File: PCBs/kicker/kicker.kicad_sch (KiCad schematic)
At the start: 1 part, among them Q1 CSD19534Q5A

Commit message: kicker actual start
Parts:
- added C1: 100n, Capacitor_SMD:C_1206_3216Metric, symbol Device:C
- added C2: 4.7u, Capacitor_SMD:C_1206_3216Metric, symbol Device:C
- added C3, C4, C5, C6: 3300u, Capacitor_THT:CP_Radial_D18.0mm_P7.50mm, symbol Device:C_Polarized
- added R1: 2, Resistor_SMD:R_0805_2012Metric, symbol Device:R
- added R2, R3: 10k, Resistor_SMD:R_0603_1608Metric, symbol Device:R
- added R4: 100, Resistor_SMD:R_0603_1608Metric, symbol Device:R
- added U1: UCC27624DR, UCC27624DR:SOIC127P599X175-8N, symbol UCC27624DR:UCC27624DR
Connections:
- net GND: now reaches Q1.1 (S), Q1.2 (S), Q1.3 (S)
- net GND: now also C1.2, C2.2, R2.2, R3.2, U1.3 (GND), U1.4 (INB), U1.8 (ENB)
- net outFET: now reaches Q1.4 (G)
- net outFET: now also R1.2, R3.1
- net SOLout: now reaches Q1.5 (D)
- new net: R2.1, R4.1, U1.2 (INA)
- new net: R1.1, U1.7 (OUTA)
- new net VCC: C1.1, C2.1, U1.1 (ENA), U1.6 (VDD)
- new net mcuDrive: R4.2
- no-connect marks 0 -> 1
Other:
- moved on the sheet: Q1

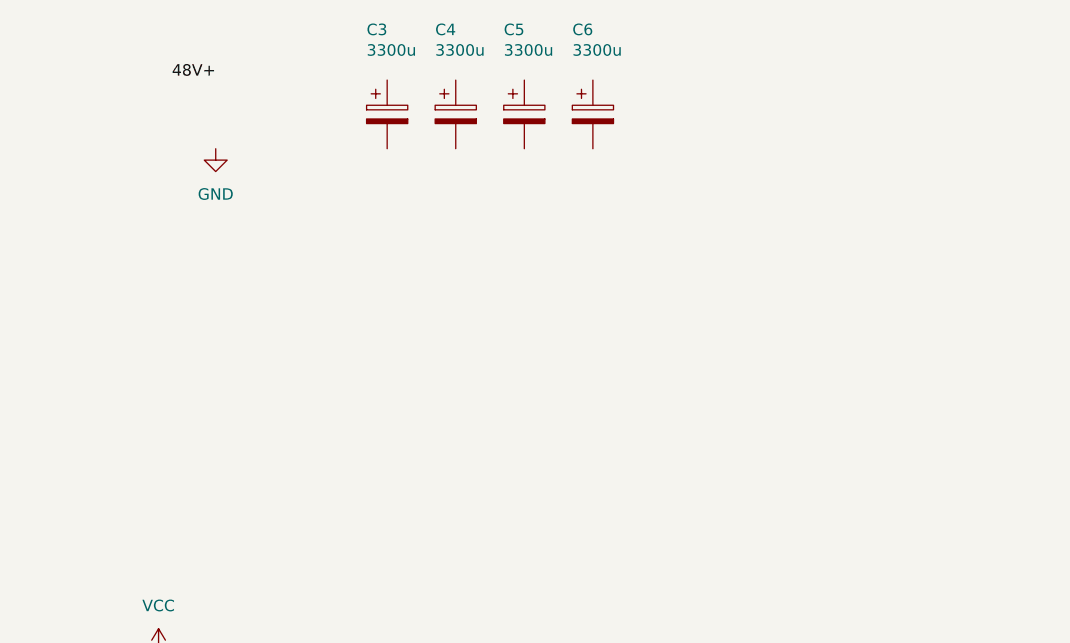
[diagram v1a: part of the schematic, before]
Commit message: fix driver footprint
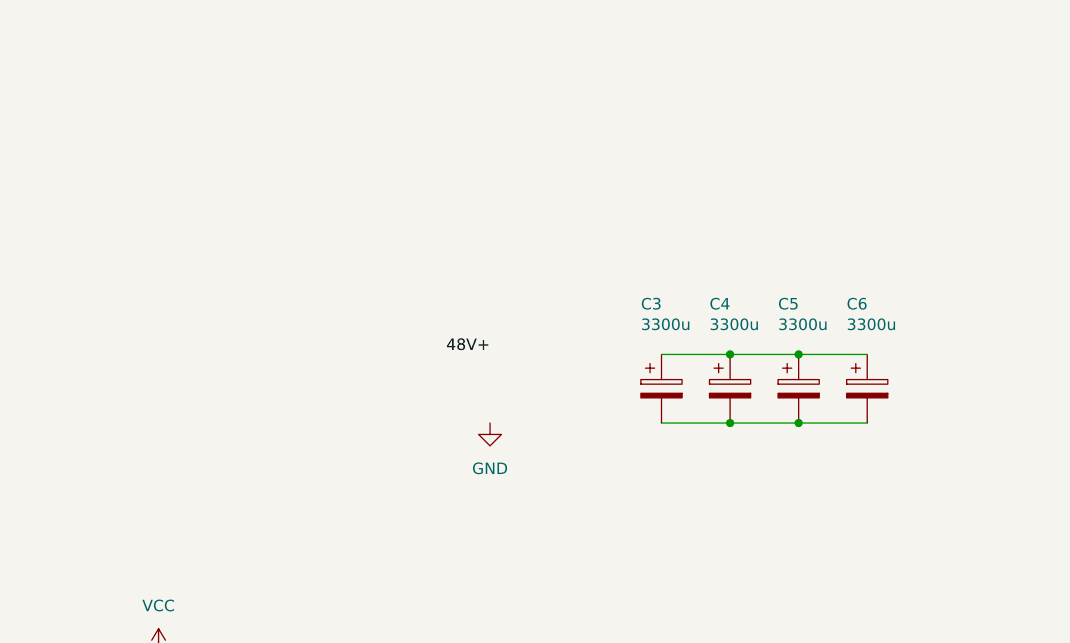
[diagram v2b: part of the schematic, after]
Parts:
- U1: footprint UCC27624DR:SOIC127P599X175-8N -> SOIC127P599X175-8N
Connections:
- net at C6.1: now also C3.1, C4.1, C5.1
- net at C6.2: now also C3.2, C4.2, C5.2
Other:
- moved on the sheet: C3, C4, C5, C6
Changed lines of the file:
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@@
+	)
+	(junction
+		(at 176.53 74.93)
+		(diameter 0)
+		(color 0 0 0 0)
+	)
+	(junction
+		(at 168.91 67.31)
+		(diameter 0)
+		(color 0 0 0 0)
 	)
 	(junction
@@
 	)
 	(junction
+		(at 168.91 74.93)
+		(diameter 0)
+		(color 0 0 0 0)
+	)
+	(junction
 		(at 88.9 156.21)
 		(diameter 0)
@@
 		(color 0 0 0 0)
 	)
+	(junction
+		(at 176.53 67.31)
+		(diameter 0)
+		(color 0 0 0 0)
+	)
 	(no_connect
 		(at 120.65 120.65)
@@
 	(wire
 		(pts
+			(xy 176.53 74.93) (xy 184.15 74.93)
+		)
+		(stroke
+			(width 0)
+			(type default)
+		)
+	)
+	(wire
+		(pts
 			(xy 109.22 156.21) (xy 123.19 156.21)
 		)
@@
 	(wire
 		(pts
+			(xy 161.29 74.93) (xy 168.91 74.93)
+		)
+		(stroke
+			(width 0)
+			(type default)
+		)
+	)
+	(wire
+		(pts
+			(xy 168.91 67.31) (xy 176.53 67.31)
+		)
+		(stroke
+			(width 0)
+			(type default)
+		)
+	)
+	(wire
+		(pts
 			(xy 105.41 146.05) (xy 105.41 144.78)
 		)
@@
 	(wire
 		(pts
+			(xy 168.91 74.93) (xy 176.53 74.93)
+		)
+		(stroke
+			(width 0)
+			(type default)
+		)
+	)
+	(wire
+		(pts
 			(xy 87.63 101.6) (xy 87.63 118.11)
 		)
@@
 	(wire
 		(pts
+			(xy 176.53 67.31) (xy 184.15 67.31)
+		)
+		(stroke
+			(width 0)
+			(type default)
+		)
+	)
+	(wire
+		(pts
+			(xy 161.29 67.31) (xy 168.91 67.31)
+		)
+		(stroke
+			(width 0)
+			(type default)
+		)
+	)
+	(wire
+		(pts
 			(xy 101.6 156.21) (xy 105.41 156.21)
 		)
@@
 	)
 	(label "48V+"
-		(at 111.76 36.83 180)
+		(at 142.24 67.31 180)
 		(effects
 			(font
@@
 	(symbol
 		(lib_id "Device:C_Polarized")
-		(at 153.67 40.64 0)
+		(at 184.15 71.12 0)
 		(unit 1)
 		(exclude_from_sim no)
@@
 		(dnp no)
 		(property "Reference" "C6"
-			(at 151.384 31.242 0)
+			(at 181.864 61.722 0)
 			(effects
 				(font
@@
 		)
 		(property "Value" "3300u"
-			(at 151.384 33.528 0)
+			(at 181.864 64.008 0)
 			(effects
 				(font
@@
 		)
 		(property "Footprint" "Capacitor_THT:CP_Radial_D18.0mm_P7.50mm"
-			(at 154.6352 44.45 0)
+			(at 185.1152 74.93 0)
 			(effects
 				(font
@@
 		)
 		(property "Datasheet" "~"
-			(at 153.67 40.64 0)
+			(at 184.15 71.12 0)
 			(effects
 				(font
@@
 		)
 		(property "Description" "Polarized capacitor"
-			(at 153.67 40.64 0)
+			(at 184.15 71.12 0)
 			(effects
 				(font
@@
 	(symbol
 		(lib_id "Device:C_Polarized")
-		(at 130.81 40.64 0)
+		(at 161.29 71.12 0)
 		(unit 1)
 		(exclude_from_sim no)
@@
 		(dnp no)
 		(property "Reference" "C3"
-			(at 128.524 31.242 0)
+			(at 159.004 61.722 0)
 			(effects
 				(font
@@
 		)
 		(property "Value" "3300u"
-			(at 128.524 33.528 0)
+			(at 159.004 64.008 0)
 			(effects
 				(font
@@
 		)
 		(property "Footprint" "Capacitor_THT:CP_Radial_D18.0mm_P7.50mm"
-			(at 131.7752 44.45 0)
+			(at 162.2552 74.93 0)
 			(effects
 				(font
@@
 		)
 		(property "Datasheet" "~"
-			(at 130.81 40.64 0)
+			(at 161.29 71.12 0)
 			(effects
 				(font
@@
 		)
 		(property "Description" "Polarized capacitor"
-			(at 130.81 40.64 0)
+			(at 161.29 71.12 0)
 			(effects
 				(font
@@
 			)
 		)
-		(property "Footprint" "UCC27624DR:SOIC127P599X175-8N"
+		(property "Footprint" "SOIC127P599X175-8N"
 			(at 105.41 123.19 0)
 			(effects
@@
 	(symbol
 		(lib_id "Device:C_Polarized")
-		(at 146.05 40.64 0)
+		(at 176.53 71.12 0)
 		(unit 1)
 		(exclude_from_sim no)
@@
 		(dnp no)
 		(property "Reference" "C5"
-			(at 143.764 31.242 0)
+			(at 174.244 61.722 0)
 			(effects
 				(font
@@
 		)
 		(property "Value" "3300u"
-			(at 143.764 33.528 0)
+			(at 174.244 64.008 0)
 			(effects
 				(font
@@
 		)
 		(property "Footprint" "Capacitor_THT:CP_Radial_D18.0mm_P7.50mm"
-			(at 147.0152 44.45 0)
+			(at 177.4952 74.93 0)
 			(effects
 				(font
@@
 		)
 		(property "Datasheet" "~"
-			(at 146.05 40.64 0)
+			(at 176.53 71.12 0)
 			(effects
 				(font
@@
 		)
 		(property "Description" "Polarized capacitor"
-			(at 146.05 40.64 0)
+			(at 176.53 71.12 0)
 			(effects
 				(font
@@
 	(symbol
 		(lib_id "power:GND")
-		(at 111.76 44.45 0)
+		(at 142.24 74.93 0)
 		(unit 1)
 		(exclude_from_sim no)
@@
 		(fields_autoplaced yes)
 		(property "Reference" "#PWR05"
-			(at 111.76 50.8 0)
+			(at 142.24 81.28 0)
 			(effects
 				(font
@@
 		)
 		(property "Value" "GND"
-			(at 111.76 49.53 0)
+			(at 142.24 80.01 0)
 			(effects
 				(font
@@
 		)
 		(property "Footprint" ""
-			(at 111.76 44.45 0)
+			(at 142.24 74.93 0)
 			(effects
 				(font
@@
 		)
 		(property "Datasheet" ""
-			(at 111.76 44.45 0)
+			(at 142.24 74.93 0)
 			(effects
 				(font
@@
 		)
 		(property "Description" "Power symbol creates a global label with name \"GND\" , ground"
-			(at 111.76 44.45 0)
+			(at 142.24 74.93 0)
 			(effects
 				(font
@@
 	(symbol
 		(lib_id "Device:C_Polarized")
-		(at 138.43 40.64 0)
+		(at 168.91 71.12 0)
 		(unit 1)
 		(exclude_from_sim no)
@@
 		(dnp no)
 		(property "Reference" "C4"
-			(at 136.144 31.242 0)
+			(at 166.624 61.722 0)
 			(effects
 				(font
@@
 		)
 		(property "Value" "3300u"
-			(at 136.144 33.528 0)
+			(at 166.624 64.008 0)
 			(effects
 				(font
@@
 		)
 		(property "Footprint" "Capacitor_THT:CP_Radial_D18.0mm_P7.50mm"
-			(at 139.3952 44.45 0)
+			(at 169.8752 74.93 0)
 			(effects
 				(font
@@
 		)
 		(property "Datasheet" "~"
-			(at 138.43 40.64 0)
+			(at 168.91 71.12 0)
 			(effects
 				(font
@@
 		)
 		(property "Description" "Polarized capacitor"
-			(at 138.43 40.64 0)
-			(effects
-				(font
+			(at 168.91 71.12 0)
+			(effects
+				(font

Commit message: kicker v0.1
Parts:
- added J1: Conn_01x02_Socket, Connector_JST:JST_XH_S2B-XH-A-1_1x02_P2.50mm_Horizontal, symbol Connector:Conn_01x02_Socket
- added J2: Conn_01x04_Socket, Connector_JST:JST_XH_S4B-XH-A-1_1x04_P2.50mm_Horizontal, symbol Connector:Conn_01x04_Socket
- added J3, J4: Conn_01x01_Socket, Connector_Wire:SolderWirePad_1x01_SMD_5x10mm, symbol Connector:Conn_01x01_Socket
- added Q2: IRF540N, Package_TO_SOT_THT:TO-220-3_Horizontal_TabDown, symbol Transistor_FET:IRF540N
- added R5: 100, Package_TO_SOT_SMD:TO-263-2, symbol Device:R
- added R6, R9: 10k, Resistor_SMD:R_0603_1608Metric, symbol Device:R
- added R7: 100, Resistor_SMD:R_0603_1608Metric, symbol Device:R
- added R8: 2, Resistor_SMD:R_0805_2012Metric, symbol Device:R
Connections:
- net 48V+: now also J1.1 (Pin_1), R5.1
- net GND: now also J1.2 (Pin_2), J2.4 (Pin_4), Q2.3 (S), R6.2, R9.2; no longer U1.4 (INB), U1.8 (ENB)
- net SOLout: now also J3.1 (Pin_1)
- net VCC: now also U1.8 (ENB), J2.3 (Pin_3)
- net mcuDrive: now also J2.2 (Pin_2)
- net at C3.1, C4.1, C5.1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: now also R5.2
- net SOLin: now reaches C3.2, C4.2, C5.2, C6.2
- net SOLin: now also J4.1 (Pin_1), Q2.2 (D)
- net at U1.5 (OUTB): now also R8.1
- new net: R6.1, R7.1, U1.4 (INB)
- new net mcuCap: J2.1 (Pin_1), R7.2
- new net outCAP: Q2.1 (G), R8.2, R9.1
- no-connect marks 1 -> 0
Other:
- moved on the sheet: C1, C2, C3, C4, C5, C6, Q1, R1, R2, R3, R4, U1

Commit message: ee
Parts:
- removed J1: Conn_01x02_Socket, Connector_JST:JST_XH_S2B-XH-A-1_1x02_P2.50mm_Horizontal, symbol Connector:Conn_01x02_Socket
- removed Q2: IRF540N, Package_TO_SOT_THT:TO-220-3_Horizontal_TabDown, symbol Transistor_FET:IRF540N
- removed R9: 10k, Resistor_SMD:R_0603_1608Metric, symbol Device:R
- added C10, C8: 220u, Capacitor_SMD:CP_Elec_10x10.5, symbol Device:C_Polarized
- added C7, C9: 1u, Capacitor_SMD:C_1206_3216Metric, symbol Device:C
- added D1: B560C, digikey-footprints:DO-214AB, symbol Device:D_Schottky
- added D2: SS210, Diode_SMD:D_SMA, symbol Device:D_Schottky
- added L1: 47u, Inductor_SMD:L_Sunlord_MWSA1206S-470, symbol Device:L_Ferrite
- added R11: 47k, Resistor_SMD:R_0603_1608Metric, symbol Device:R
- added R12: 2k, Resistor_SMD:R_0603_1608Metric, symbol Device:R
- added RV1: 50k, Potentiometer_THT:Potentiometer_Bourns_3296W_Vertical, symbol Device:R_Potentiometer_Trim
- added U2: XL6019E1, Package_TO_SOT_SMD:TO-263-5_TabPin3, symbol New_Library:XL6019E1
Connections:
- net SOLin is gone; now on net GND: C3.2, C4.2, C5.2, C6.2, J4.1 (Pin_1)
- net 48V+: now also D2.1 (K)
- net GND: now also C10.2, C7.2, C8.2, C9.2, R12.2, U2.1 (GND)
- net VCC: now also C7.1, C8.1, L1.1, U2.4 (VIN)
- net mcuDrive renamed mcuKick
- net outCAP renamed capEN
- net capEN: now also U2.2 (EN)
- new net: C10.1, C9.1, D1.1 (K), D2.2 (A), R11.1
- new net: D1.2 (A), L1.2, U2.3 (SW)
- new net: R12.1, RV1.2, RV1.3, U2.5 (FB)
- new net: R11.2, RV1.1
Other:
- note added: "16V to 48V boost"
- moved on the sheet: C1, C2, C3, C4, C5, C6, J2, J3, J4, Q1, R1, R2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

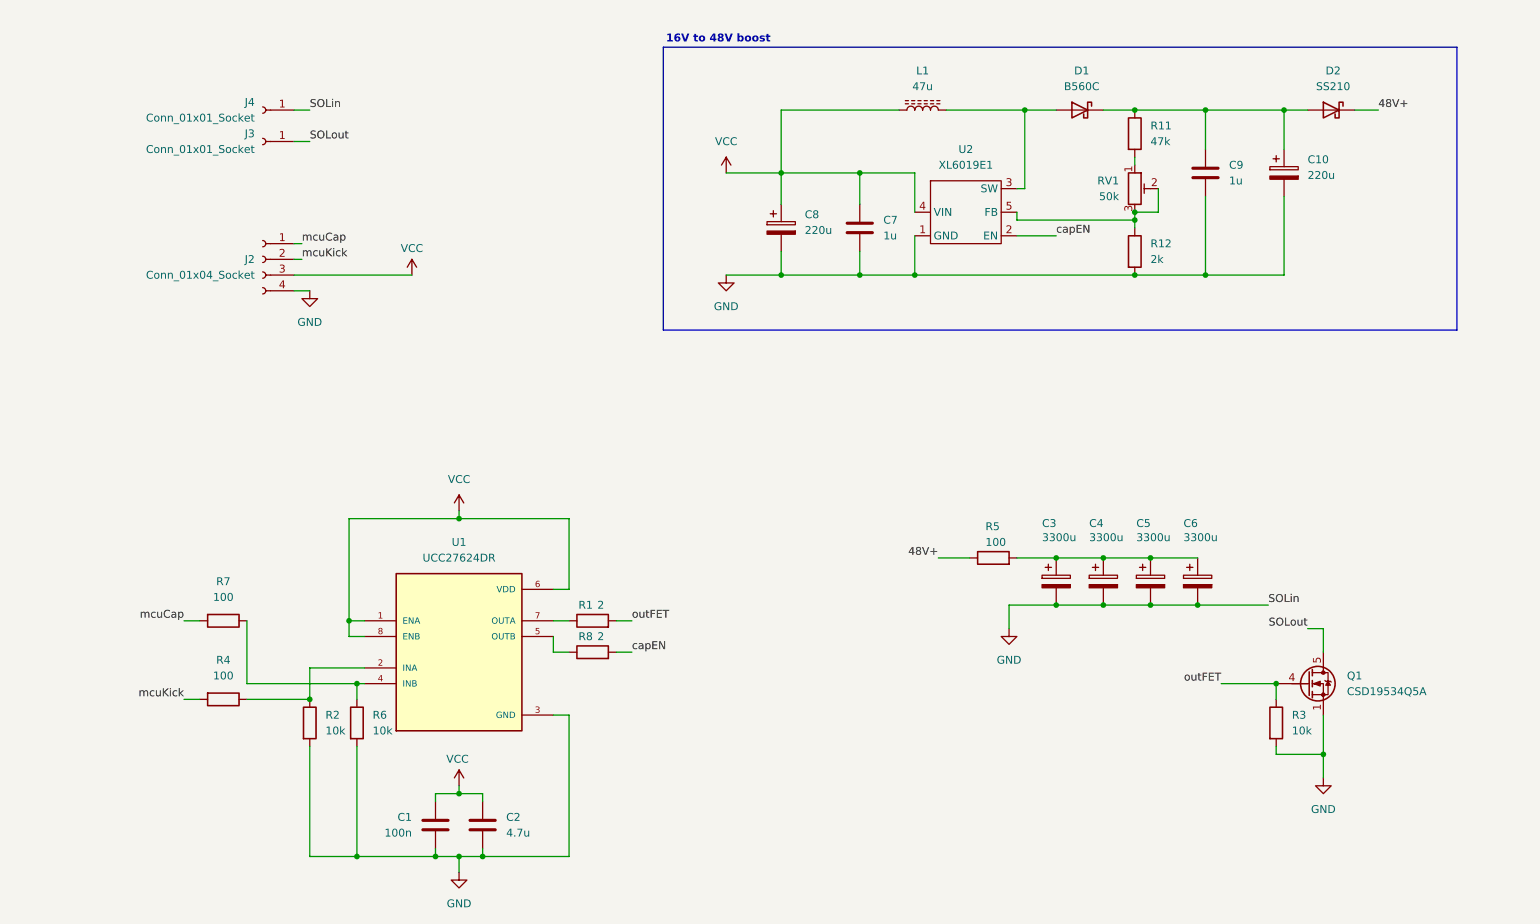
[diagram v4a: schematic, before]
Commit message: kicker schematic reorganise
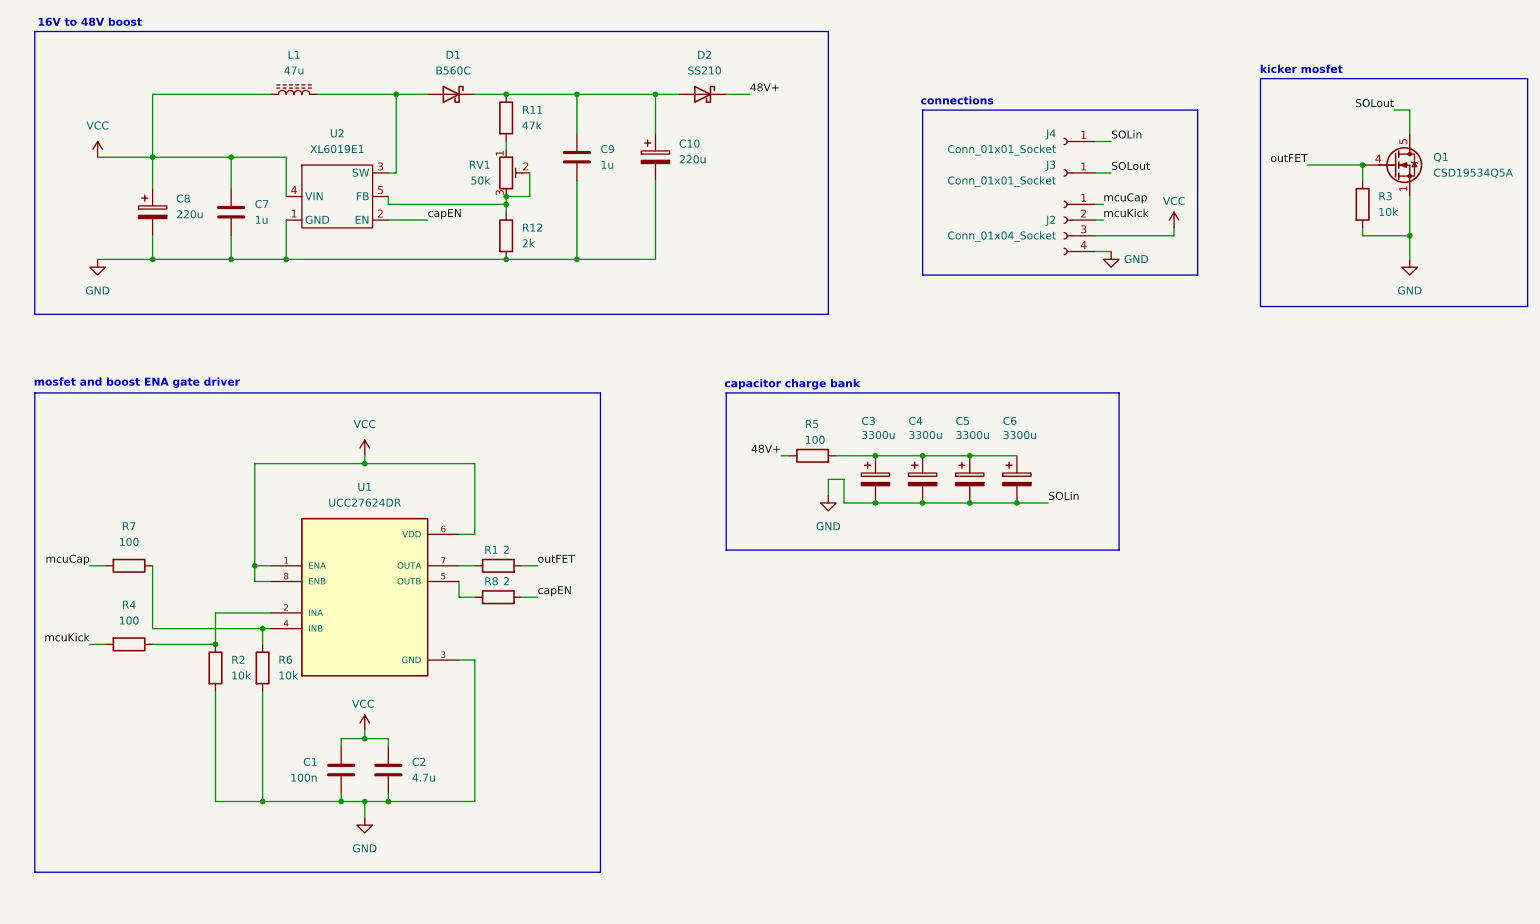
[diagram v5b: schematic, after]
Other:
- note added: "capacitor charge bank"
- note added: "connections"
- note added: "kicker mosfet"
- note added: "mosfet and boost ENA gate driver"
- moved on the sheet: C1, C10, C2, C3, C4, C5, C6, C7, C8, C9, D1, D2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

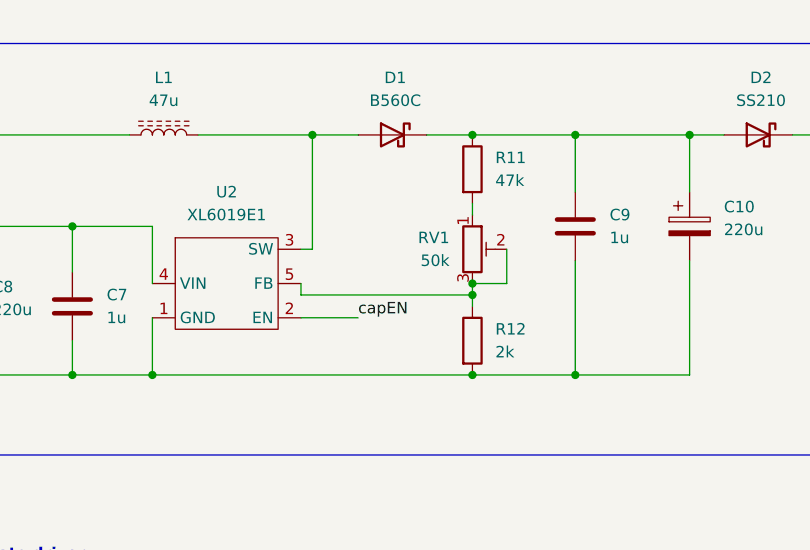
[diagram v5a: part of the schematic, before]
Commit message: kicker board and outline
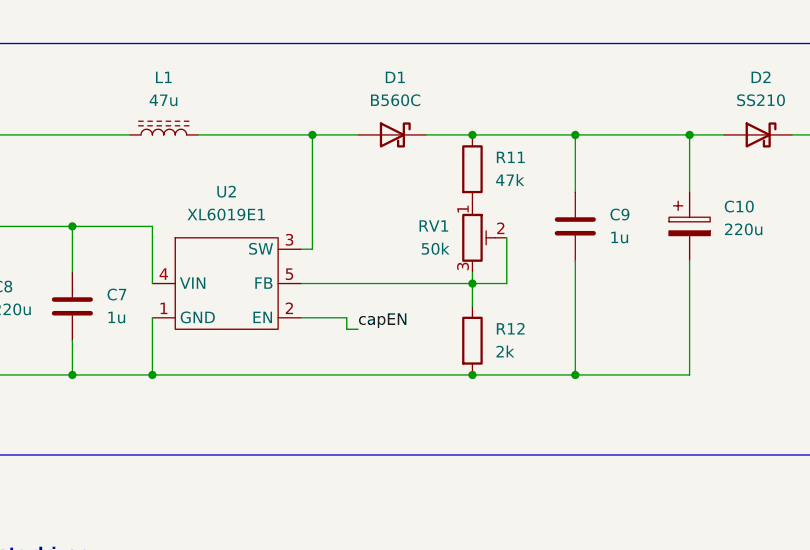
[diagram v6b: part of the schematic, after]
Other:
- moved on the sheet: RV1
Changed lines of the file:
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@@
-	)
-	(junction
-		(at 106.68 60.96)
-		(diameter 0)
-		(color 0 0 0 0)
 	)
 	(junction
@@
 	(wire
 		(pts
+			(xy 106.68 58.42) (xy 106.68 59.69)
+		)
+		(stroke
+			(width 0)
+			(type default)
+		)
+	)
+	(wire
+		(pts
 			(xy 62.23 69.85) (xy 49.53 69.85)
 		)
@@
 	(wire
 		(pts
-			(xy 106.68 52.07) (xy 106.68 50.8)
+			(xy 92.71 64.77) (xy 92.71 63.5)
 		)
 		(stroke
@@
 	(wire
 		(pts
-			(xy 106.68 62.23) (xy 106.68 60.96)
-		)
-		(stroke
-			(width 0)
-			(type default)
-		)
-	)
-	(wire
-		(pts
 			(xy 68.58 43.18) (xy 49.53 43.18)
 		)
@@
 	(wire
 		(pts
-			(xy 87.63 60.96) (xy 87.63 59.69)
-		)
-		(stroke
-			(width 0)
-			(type default)
-		)
-	)
-	(wire
-		(pts
 			(xy 83.82 157.48) (xy 87.63 157.48)
 		)
@@
 	(wire
 		(pts
-			(xy 87.63 60.96) (xy 106.68 60.96)
+			(xy 87.63 59.69) (xy 106.68 59.69)
 		)
 		(stroke
@@
 	(wire
 		(pts
-			(xy 110.49 55.88) (xy 110.49 59.69)
+			(xy 92.71 63.5) (xy 87.63 63.5)
+		)
+		(stroke
+			(width 0)
+			(type default)
+		)
+	)
+	(wire
+		(pts
+			(xy 110.49 54.61) (xy 110.49 59.69)
 		)
 		(stroke
@@
 	(wire
 		(pts
-			(xy 87.63 63.5) (xy 93.98 63.5)
+			(xy 92.71 64.77) (xy 93.98 64.77)
+		)
+		(stroke
+			(width 0)
+			(type default)
+		)
+	)
+	(wire
+		(pts
+			(xy 106.68 59.69) (xy 106.68 62.23)
 		)
 		(stroke
@@
 		(pts
 			(xy 173.99 109.22) (xy 181.61 109.22)
-		)
-		(stroke
-			(width 0)
-			(type default)
-		)
-	)
-	(wire
-		(pts
-			(xy 106.68 59.69) (xy 106.68 60.96)
 		)
 		(stroke
@@
 	)
 	(label "capEN"
-		(at 93.98 63.5 0)
+		(at 93.98 64.77 0)
 		(effects
 			(font
@@
 	(symbol
 		(lib_id "Device:R_Potentiometer_Trim")
-		(at 106.68 55.88 0)
+		(at 106.68 54.61 0)
 		(unit 1)
 		(exclude_from_sim no)
@@
 		(fields_autoplaced yes)
 		(property "Reference" "RV1"
-			(at 104.14 54.6099 0)
+			(at 104.14 53.3399 0)
 			(effects
 				(font
@@
 		)
 		(property "Value" "50k"
-			(at 104.14 57.1499 0)
+			(at 104.14 55.8799 0)
 			(effects
 				(font
@@
 		)
 		(property "Footprint" "Potentiometer_THT:Potentiometer_Bourns_3296W_Vertical"
-			(at 106.68 55.88 0)
+			(at 106.68 54.61 0)
 			(effects
 				(font
@@
 		)
 		(property "Datasheet" "~"
-			(at 106.68 55.88 0)
+			(at 106.68 54.61 0)
 			(effects
 				(font
@@
 		)
 		(property "Description" "Trim-potentiometer"
-			(at 106.68 55.88 0)
-			(effects
-				(font
+			(at 106.68 54.61 0)
+			(effects
+				(font
